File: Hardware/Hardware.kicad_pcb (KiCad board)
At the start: 2 copper layers, 91.4 x 142.2 mm, 46 parts, among them J1 Conn_01x04_Pin, J2 RJ45_LED_Shielded, J3 USB_A, SW1 SW_SPST, SW2 SW_Push, SW3 SW_Push, SW4 SW_Push, SW5 SW_Push, SW6 SW_Push, SW7 SW_Push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

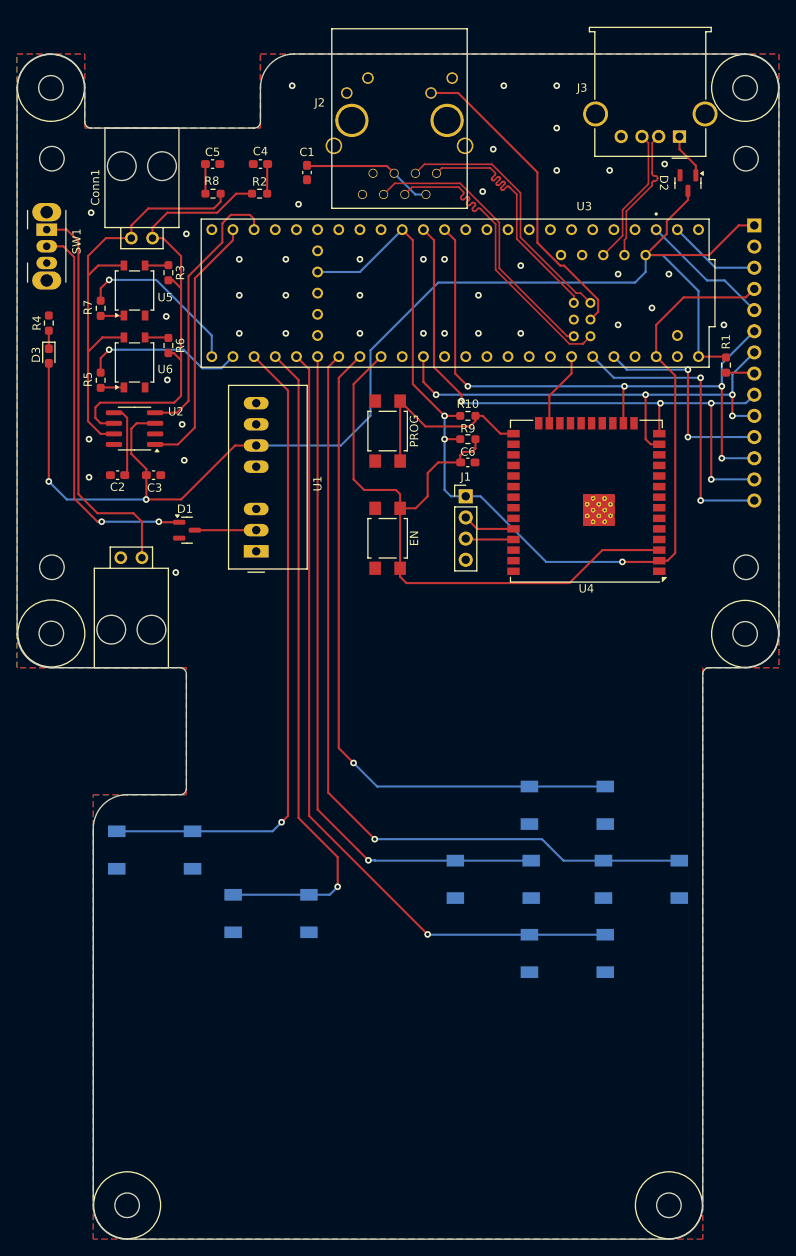
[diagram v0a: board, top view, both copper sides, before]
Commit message: changed battery case to through-hole pcb mount
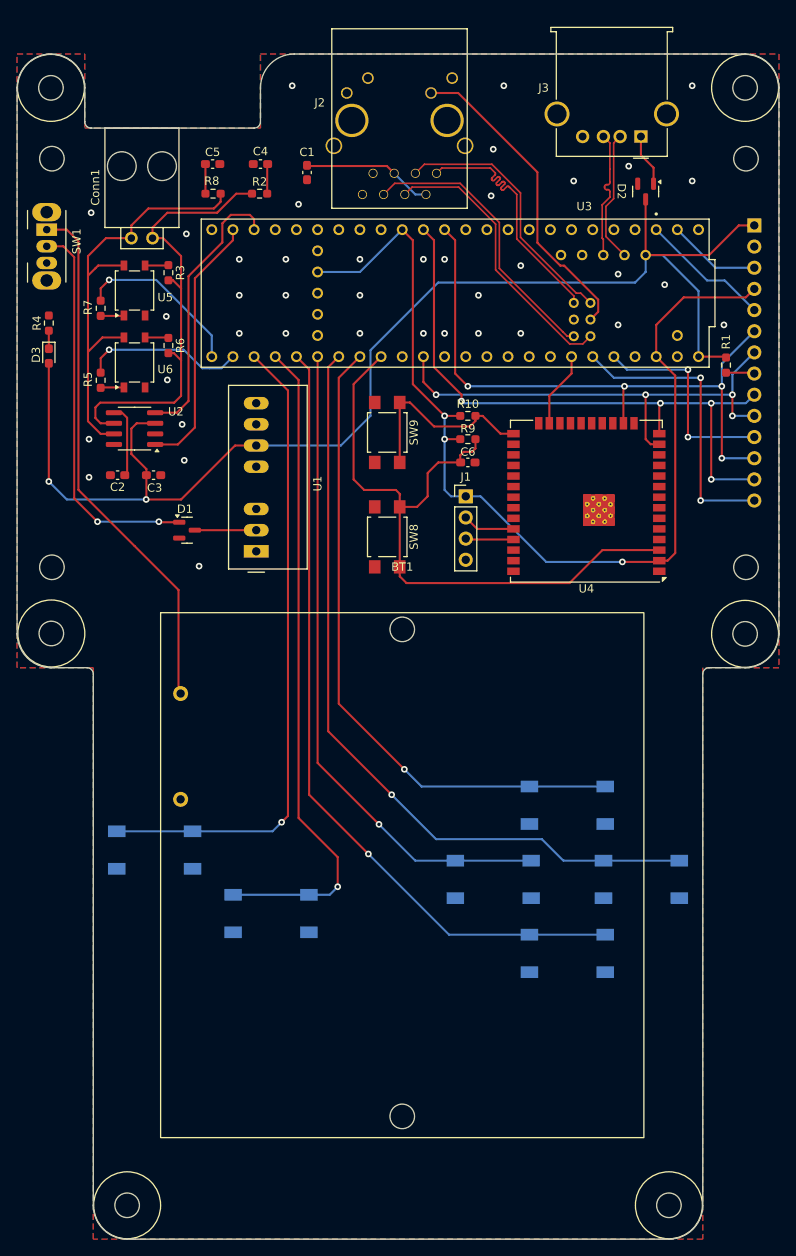
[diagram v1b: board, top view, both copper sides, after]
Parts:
- removed EN, PROG: SW_Push, Button_Switch_SMD:SW_SPST_TL3305A
- added SW8: SW_Push, Button_Switch_SMD:SW_SPST_TL3305A, F.Cu at (198.1, 118.9)
- added SW9: SW_Push, Button_Switch_SMD:SW_SPST_TL3305A, F.Cu at (198.1, 106.4)
- BT1: footprint MRDT_Connectors:MOLEX_SL_02_Horizontal -> Tester:Bat_4xAA_MP000327
- moved BT1 31.9 mm to (199.9, 128.0), turned to 0 degrees
- moved D2 5.18 mm to (229.1, 77.5)
- moved J3 4.63 mm to (228.5, 70.9)
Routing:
- net Net-(BT1-+): track 48.0 -> 63.7 mm
- net KP_LEFT: track 98.4 -> 94.1 mm
- net Rx+: track 37.7 -> 34.1 mm
- net KP_RIGHT: track 82.5 -> 79.3 mm
- net KP_UP: track 81.9 -> 78.8 mm
- net +5V: track 161.0 -> 157.9 mm
- net KP_DOWN: track 97.2 -> 95.7 mm
- net USB_D+: track 16.8 -> 15.8 mm
- net USB_D-: track 16.8 -> 15.9 mm
- net Net-(D2-A): track 5.46 -> 6.29 mm
- net GND: vias 41 -> 39
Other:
- outline, holes or cut-outs redrawn

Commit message: Update Hardware.kicad_pcb
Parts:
- added G***: LOGO, MRDT_Silkscreens:0_MRDT_Logo_10mm, F.Cu at (181.0, 61.5)
- moved D3 1.60 mm to (157.5, 98.8)
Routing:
- net Net-(D3-K): track 2.16 -> 3.76 mm
- net +5V: track 157.9 -> 156.3 mm
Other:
- board text added: "Enter"
- board text added: "ROVE BOY"
- board text added: "Tester Board, Rev 1 Mars Rover, 2024 Missouri S&T Adam Klassen, Donovan Yavitz"
- board text removed: "Accept"
